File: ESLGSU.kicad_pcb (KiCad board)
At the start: 6 copper layers, 90.9 x 99.5 mm, 297 parts, among them J1 PJ-080BH, Q1 DMN67D7L-7, Q2 DMN67D7L-7, Q3 DMN67D7L-7, Q4 DMN67D7L-7, Q5 DMN67D7L-7, Q6 DMN67D7L-7, U1 TCA9544APWR, U10 TPS259474LRPWR, U11 LM73100RPWR, U12 MP28167-A, U13 INA219AIDCNR, U14 TPS259474LRPWR, U15 LM73100RPWR, U16 MP28167-A, U17 INA219AIDCNR, U18 TPS259474LRPWR, U19 LM73100RPWR, U2 DMT3006LDK-7, U20 MP28167-A, U21 INA219AIDCNR, U22 TPS259474LRPWR, U23 LM73100RPWR, U24 MP28167-A, U25 M20-7812045, U26 AP63203WU-7, U27 AP63205WU-7, U28 TPS2121RUXR, U29 TCAN1051GVDRBRQ, U3 INA219AIDCNR, U30 THVD1450DRBR, U31 TMUX1574RSVR, U32 TMUX1574RSVR, U33 TXU0202DTTR, U34 TMUX1574RSVR, U35 TXU0202DTTR, U36 TXB0104RUT, U37 STM32H753ZIT6, U38 STM32F072VBT6, U39 PCA9306, U4 DML3012LDC-7, U40 TXB0104RUT, U41 STM32F072CBUx, U44 TMUX1574RSVR, U46 TXB0104RUT, U47 TMUX1574RSVR, U5 AP74700QW6-7, U6 DMT3006LDK-7, U7 DML3012LDC-7, U8 AP74700QW6-7, U9 INA219AIDCNR

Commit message: Last tweaks on schematic
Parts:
- added C101: 22u, Capacitor_SMD:C_0805_2012Metric, F.Cu at (-123.8, -157.2)
- added C102: 100n, Capacitor_SMD:C_0402_1005Metric, F.Cu at (-121.5, -163.4)
- added C108: 100n, Capacitor_SMD:C_0402_1005Metric, F.Cu at (256.5, 49.3)
- added C109: 100n, Capacitor_SMD:C_0402_1005Metric, F.Cu at (256.5, 51.3)
- added C112: 100n, Capacitor_SMD:C_0402_1005Metric, F.Cu at (256.5, 53.2)
- added C113: 100n, Capacitor_SMD:C_0402_1005Metric, F.Cu at (256.5, 55.2)
- added C114: 100n, Capacitor_SMD:C_0402_1005Metric, F.Cu at (256.5, 57.2)
- added C115: 100p, Capacitor_SMD:C_0402_1005Metric, F.Cu at (256.5, 59.1)
- added C116: 2.2u, Capacitor_SMD:C_0402_1005Metric, F.Cu at (259.4, 49.3)
- added C117: 100n, Capacitor_SMD:C_0402_1005Metric, F.Cu at (259.4, 51.3)
- added C118: 100n, Capacitor_SMD:C_0402_1005Metric, F.Cu at (259.4, 53.2)
- added C119: 100n, Capacitor_SMD:C_0402_1005Metric, F.Cu at (259.4, 55.2)
- added C120: 4.7u, Capacitor_SMD:C_0402_1005Metric, F.Cu at (259.4, 57.2)
- added C121: 1u, Capacitor_SMD:C_0402_1005Metric, F.Cu at (259.4, 59.1)
- added C122: 100n, Capacitor_SMD:C_0402_1005Metric, F.Cu at (262.2, 49.3)
- added C123: 100n, Capacitor_SMD:C_0402_1005Metric, F.Cu at (262.2, 51.3)
- added C124: 100n, Capacitor_SMD:C_0402_1005Metric, F.Cu at (262.2, 53.2)
- added C125: 100n, Capacitor_SMD:C_0402_1005Metric, F.Cu at (262.2, 55.2)
- added C126: 100n, Capacitor_SMD:C_0402_1005Metric, F.Cu at (262.2, 57.2)
- added C127: 100n, Capacitor_SMD:C_0402_1005Metric, F.Cu at (249.5, 117.4)
- added C128: 100n, Capacitor_SMD:C_0402_1005Metric, F.Cu at (249.5, 119.4)
- added C129: 100n, Capacitor_SMD:C_0402_1005Metric, F.Cu at (249.5, 121.4)
- added C130: 100n, Capacitor_SMD:C_0402_1005Metric, F.Cu at (249.5, 123.3)
- added C131: 100n, Capacitor_SMD:C_0402_1005Metric, F.Cu at (249.5, 125.3)
- added C132: 100n, Capacitor_SMD:C_0402_1005Metric, F.Cu at (249.5, 127.3)
- added C133: 100n, Capacitor_SMD:C_0402_1005Metric, F.Cu at (249.5, 129.2)
- added C134: 100p, Capacitor_SMD:C_0402_1005Metric, F.Cu at (252.4, 117.4)
- added C135: 2.2u, Capacitor_SMD:C_0402_1005Metric, F.Cu at (252.4, 119.4)
- added C136: 100n, Capacitor_SMD:C_0402_1005Metric, F.Cu at (252.4, 121.4)
- added C137: 100n, Capacitor_SMD:C_0402_1005Metric, F.Cu at (252.4, 123.3)
- added C138: 100n, Capacitor_SMD:C_0402_1005Metric, F.Cu at (252.4, 125.3)
- added C139: 4.7u, Capacitor_SMD:C_0402_1005Metric, F.Cu at (252.4, 127.3)
- added C140: 1u, Capacitor_SMD:C_0402_1005Metric, F.Cu at (252.4, 129.2)
- added C141: 100n, Capacitor_SMD:C_0402_1005Metric, F.Cu at (255.3, 117.4)
- added C142: 100n, Capacitor_SMD:C_0402_1005Metric, F.Cu at (255.3, 119.4)
- added C143: 100n, Capacitor_SMD:C_0402_1005Metric, F.Cu at (255.3, 121.4)
- added C144: 100n, Capacitor_SMD:C_0402_1005Metric, F.Cu at (255.3, 123.3)
- added C145: 100n, Capacitor_SMD:C_0402_1005Metric, F.Cu at (255.3, 125.3)
- added C146: 100n, Capacitor_SMD:C_0402_1005Metric, F.Cu at (160.4, 69.4)
- added C147: 100n, Capacitor_SMD:C_0402_1005Metric, F.Cu at (160.4, 71.4)
- added C148: 100n, Capacitor_SMD:C_0402_1005Metric, F.Cu at (160.4, 73.3)
- added C149: 100n, Capacitor_SMD:C_0402_1005Metric, F.Cu at (160.4, 75.3)
- added C150: 100n, Capacitor_SMD:C_0402_1005Metric, F.Cu at (160.4, 77.3)
- added C151: 100n, Capacitor_SMD:C_0402_1005Metric, F.Cu at (160.4, 79.2)
- added C152: 100n, Capacitor_SMD:C_0402_1005Metric, F.Cu at (160.4, 81.2)
- added C153: 100n, Capacitor_SMD:C_0402_1005Metric, F.Cu at (160.4, 83.2)
- added C154: 100n, Capacitor_SMD:C_0402_1005Metric, F.Cu at (163.2, 69.4)
- added C155: 100n, Capacitor_SMD:C_0402_1005Metric, F.Cu at (163.2, 71.4)
- added C156: 100n, Capacitor_SMD:C_0402_1005Metric, F.Cu at (163.2, 73.3)
- added C157: 100n, Capacitor_SMD:C_0402_1005Metric, F.Cu at (163.2, 75.3)
- added C158: 100n, Capacitor_SMD:C_0402_1005Metric, F.Cu at (163.2, 77.3)
- added C159: 100p, Capacitor_SMD:C_0402_1005Metric, F.Cu at (163.2, 79.2)
- added C160: 100p, Capacitor_SMD:C_0402_1005Metric, F.Cu at (163.2, 81.2)
- added C161: 100n, Capacitor_SMD:C_0402_1005Metric, F.Cu at (163.2, 83.2)
- added C162: 100n, Capacitor_SMD:C_0402_1005Metric, F.Cu at (166.1, 69.4)
- added C163: 100n, Capacitor_SMD:C_0402_1005Metric, F.Cu at (166.1, 71.4)
- added C164: 100n, Capacitor_SMD:C_0402_1005Metric, F.Cu at (166.1, 73.3)
- added C165: 100n, Capacitor_SMD:C_0402_1005Metric, F.Cu at (166.1, 75.3)
- added C166: 100n, Capacitor_SMD:C_0402_1005Metric, F.Cu at (166.1, 77.3)
- added C167: 100n, Capacitor_SMD:C_0402_1005Metric, F.Cu at (166.1, 79.2)
- added C168: 100n, Capacitor_SMD:C_0402_1005Metric, F.Cu at (166.1, 81.2)
- added C169: 100n, Capacitor_SMD:C_0402_1005Metric, F.Cu at (166.1, 83.2)
- added C170: 100n, Capacitor_SMD:C_0402_1005Metric, F.Cu at (169.0, 69.4)
- added C171: 100n, Capacitor_SMD:C_0402_1005Metric, F.Cu at (169.0, 71.4)
- added C172: 100n, Capacitor_SMD:C_0402_1005Metric, F.Cu at (169.0, 73.3)
- added C173: 100n, Capacitor_SMD:C_0402_1005Metric, F.Cu at (169.0, 75.3)
- added C174: 100n, Capacitor_SMD:C_0402_1005Metric, F.Cu at (169.0, 77.3)
- added C175: 1u, Capacitor_SMD:C_0402_1005Metric, F.Cu at (169.0, 79.2)
- added C176: 100n, Capacitor_SMD:C_0402_1005Metric, F.Cu at (169.0, 81.2)
- added C177: 100n, Capacitor_SMD:C_0402_1005Metric, F.Cu at (169.0, 83.2)
- added C178: 4.7u, Capacitor_SMD:C_0402_1005Metric, F.Cu at (171.9, 69.4)
- added C179: 1u, Capacitor_SMD:C_0402_1005Metric, F.Cu at (171.9, 71.4)
- added C180: 100n, Capacitor_SMD:C_0402_1005Metric, F.Cu at (171.9, 73.3)
- added C181: 100n, Capacitor_SMD:C_0402_1005Metric, F.Cu at (171.9, 75.3)
- added C182: 100n, Capacitor_SMD:C_0402_1005Metric, F.Cu at (171.9, 77.3)
- added C183: 100n, Capacitor_SMD:C_0402_1005Metric, F.Cu at (171.9, 79.2)
- added C184: 100n, Capacitor_SMD:C_0402_1005Metric, F.Cu at (171.9, 81.2)
- added C185: 2.2u, Capacitor_SMD:C_0402_1005Metric, F.Cu at (171.9, 83.2)
- added C186: 2.2u, Capacitor_SMD:C_0402_1005Metric, F.Cu at (174.7, 69.4)
- added C187: 100n, Capacitor_SMD:C_0402_1005Metric, F.Cu at (174.7, 71.4)
- added C188: 100n, Capacitor_SMD:C_0402_1005Metric, F.Cu at (174.7, 73.3)
- added C189: 100n, Capacitor_SMD:C_0402_1005Metric, F.Cu at (174.7, 75.3)
- added C190: 100n, Capacitor_SMD:C_0402_1005Metric, F.Cu at (174.7, 77.3)
- added C191: 100n, Capacitor_SMD:C_0402_1005Metric, F.Cu at (174.7, 79.2)
- added C192: 100n, Capacitor_SMD:C_0402_1005Metric, F.Cu at (174.7, 81.2)
- added C193: 100n, Capacitor_SMD:C_0402_1005Metric, F.Cu at (174.7, 83.2)
- added C194: 100n, Capacitor_SMD:C_0402_1005Metric, F.Cu at (391.8, 101.6)
- added C195: 100n, Capacitor_SMD:C_0402_1005Metric, F.Cu at (391.8, 103.6)
- added C196: 100n, Capacitor_SMD:C_0402_1005Metric, F.Cu at (160.4, 127.5)
- added C197: 100n, Capacitor_SMD:C_0402_1005Metric, F.Cu at (160.4, 129.5)
- added C198: 100n, Capacitor_SMD:C_0402_1005Metric, F.Cu at (160.4, 131.4)
- added C199: 100n, Capacitor_SMD:C_0402_1005Metric, F.Cu at (160.4, 133.4)
- added C200: 100n, Capacitor_SMD:C_0402_1005Metric, F.Cu at (160.4, 135.4)
- added C201: 100n, Capacitor_SMD:C_0402_1005Metric, F.Cu at (160.4, 137.3)
- added C202: 100p, Capacitor_SMD:C_0402_1005Metric, F.Cu at (160.4, 139.3)
- added C203: 100n, Capacitor_SMD:C_0402_1005Metric, F.Cu at (163.2, 123.6)
- added C204: 100n, Capacitor_SMD:C_0402_1005Metric, F.Cu at (163.2, 125.5)
- added C205: 100n, Capacitor_SMD:C_0402_1005Metric, F.Cu at (163.2, 127.5)
- added C206: 100n, Capacitor_SMD:C_0402_1005Metric, F.Cu at (163.2, 129.5)
- added C207: 100n, Capacitor_SMD:C_0402_1005Metric, F.Cu at (163.2, 131.4)
- added C208: 100n, Capacitor_SMD:C_0402_1005Metric, F.Cu at (163.2, 133.4)
- added C209: 100n, Capacitor_SMD:C_0402_1005Metric, F.Cu at (163.2, 135.4)
- added C210: 100n, Capacitor_SMD:C_0402_1005Metric, F.Cu at (163.2, 137.3)
- added C211: 1u, Capacitor_SMD:C_0402_1005Metric, F.Cu at (163.2, 139.3)
- added C212: 100n, Capacitor_SMD:C_0402_1005Metric, F.Cu at (166.1, 123.6)
- added C213: 100n, Capacitor_SMD:C_0402_1005Metric, F.Cu at (166.1, 125.5)
- added C214: 4.7u, Capacitor_SMD:C_0402_1005Metric, F.Cu at (166.1, 127.5)
- added C215: 1u, Capacitor_SMD:C_0402_1005Metric, F.Cu at (166.1, 129.5)
- added C216: 100n, Capacitor_SMD:C_0402_1005Metric, F.Cu at (166.1, 131.4)
- added C217: 100n, Capacitor_SMD:C_0402_1005Metric, F.Cu at (166.1, 133.4)
- added C218: 100n, Capacitor_SMD:C_0402_1005Metric, F.Cu at (166.1, 135.4)
- added C219: 100n, Capacitor_SMD:C_0402_1005Metric, F.Cu at (166.1, 137.3)
- added C220: 100n, Capacitor_SMD:C_0402_1005Metric, F.Cu at (166.1, 139.3)
- added C221: 2.2u, Capacitor_SMD:C_0402_1005Metric, F.Cu at (169.0, 123.6)
- added C222: 2.2u, Capacitor_SMD:C_0402_1005Metric, F.Cu at (169.0, 125.5)
- added C223: 100n, Capacitor_SMD:C_0402_1005Metric, F.Cu at (169.0, 127.5)
- added C224: 100n, Capacitor_SMD:C_0402_1005Metric, F.Cu at (169.0, 129.5)
- added C225: 100n, Capacitor_SMD:C_0402_1005Metric, F.Cu at (169.0, 131.4)
- added C226: 100n, Capacitor_SMD:C_0402_1005Metric, F.Cu at (169.0, 133.4)
- added C227: 100n, Capacitor_SMD:C_0402_1005Metric, F.Cu at (169.0, 135.4)
- added C228: 100n, Capacitor_SMD:C_0402_1005Metric, F.Cu at (169.0, 137.3)
- added C229: 100n, Capacitor_SMD:C_0402_1005Metric, F.Cu at (169.0, 139.3)
- added C230: 100n, Capacitor_SMD:C_0402_1005Metric, F.Cu at (258.3, 101.0)
- added D10: TZ-P2-0603GTCS1-0.6T, LED_SMD:LED_0603_1608Metric, F.Cu at (258.6, 131.5)
- added D11: 1N5819, Diode_SMD:D_SOD-323, F.Cu at (185.2, 66.1)
- added D12: TZ-P2-0603GTCS1-0.6T, LED_SMD:LED_0603_1608Metric, F.Cu at (202.6, 78.0)
- added D13: 1N5819, Diode_SMD:D_SOD-323, F.Cu at (185.2, 116.3)
- added D14: TZ-P2-0603GTCS1-0.6T, LED_SMD:LED_0603_1608Metric, F.Cu at (194.5, 119.7)
- added D7: 1N5819, Diode_SMD:D_SOD-323, F.Cu at (245.3, 46.2)
- added D8: TZ-P2-0603GTCS1-0.6T, LED_SMD:LED_0603_1608Metric, F.Cu at (250.4, 65.5)
- added D9: 1N5819, Diode_SMD:D_SOD-323, F.Cu at (250.0, 114.3)
- added J10: 1054301108, ESLGSU_Parts_Lib:MOLEX_1054301108, F.Cu at (220.3, 129.6)
- added J2: XT60U-M, ESLGSU_Parts_Lib:XT60, F.Cu at (134.5, -164.7)
- added J3: Conn_01x06_Pin, Connector_PinHeader_1.27mm:PinHeader_1x06_P1.27mm_Vertical_SMD_Pin1Right, F.Cu at (259.1, 65.0)
- added J4: Conn_01x06_Pin, Connector_PinHeader_1.27mm:PinHeader_1x06_P1.27mm_Vertical_SMD_Pin1Right, F.Cu at (240.5, 133.0)
- added J5: 10118194-0001LF, ESLGSU_Parts_Lib:AMPHENOL_10118194-0001LF, F.Cu at (181.0, 73.2)
- added J6: Conn_01x06_Pin, Connector_PinHeader_1.27mm:PinHeader_1x06_P1.27mm_Vertical_SMD_Pin1Right, F.Cu at (180.2, 85.8)
- added J7: 10118194-0001LF, ESLGSU_Parts_Lib:AMPHENOL_10118194-0001LF, F.Cu at (185.8, 131.7)
- added J8: Conn_01x06_Pin, Connector_PinHeader_1.27mm:PinHeader_1x06_P1.27mm_Vertical_SMD_Pin1Right, F.Cu at (174.4, 139.5)
- added J9: AMPHENOL_62684-401100ALF, ESLGSU_Parts_Lib:AMPHENOL_62684-401100ALF, F.Cu at (220.5, 117.7)
- added L7: SRP1038A-4R7M, Inductor_SMD:L_Vishay_IHLP-4040, F.Cu at (-129.8, -164.5)
- added R101: 4.7K, Resistor_SMD:R_0402_1005Metric, F.Cu at (-121.5, -165.4)
- added R102: 200K, Resistor_SMD:R_0402_1005Metric, F.Cu at (244.9, 49.3)
- added R104: 0R, Resistor_SMD:R_0402_1005Metric, F.Cu at (244.9, 51.3)
- added R105: 100K, Resistor_SMD:R_0402_1005Metric, F.Cu at (244.9, 53.3)
- added R106: 200K, Resistor_SMD:R_0402_1005Metric, F.Cu at (244.9, 55.3)
- added R107: 200K, Resistor_SMD:R_0402_1005Metric, F.Cu at (244.9, 57.3)
- added R108: 200K, Resistor_SMD:R_0402_1005Metric, F.Cu at (244.9, 59.3)
- added R109: 0R, Resistor_SMD:R_0402_1005Metric, F.Cu at (244.9, 61.2)
- added R110: 0R, Resistor_SMD:R_0402_1005Metric, F.Cu at (244.9, 63.2)
- added R111: 0R, Resistor_SMD:R_0402_1005Metric, F.Cu at (247.8, 49.3)
- added R112: 510R, Resistor_SMD:R_0402_1005Metric, F.Cu at (247.8, 51.3)
- added R113: 0R, Resistor_SMD:R_0402_1005Metric, F.Cu at (247.8, 53.3)
- added R115: 200K, Resistor_SMD:R_0402_1005Metric, F.Cu at (247.8, 55.3)
- added R116: 200K, Resistor_SMD:R_0402_1005Metric, F.Cu at (247.8, 57.3)
- added R117: 200K, Resistor_SMD:R_0402_1005Metric, F.Cu at (247.8, 59.3)
- added R120: 10K, Resistor_SMD:R_0402_1005Metric, F.Cu at (247.8, 61.2)
- added R121: 0R, Resistor_SMD:R_0402_1005Metric, F.Cu at (247.8, 63.2)
- added R122: 10K, Resistor_SMD:R_0402_1005Metric, F.Cu at (250.7, 49.3)
- added R123: 10K, Resistor_SMD:R_0402_1005Metric, F.Cu at (250.7, 51.3)
- added R124: 510R, Resistor_SMD:R_0402_1005Metric, F.Cu at (250.7, 53.3)
- added R125: 0R, Resistor_SMD:R_0402_1005Metric, F.Cu at (250.7, 55.3)
- added R126: 200K, Resistor_SMD:R_0402_1005Metric, F.Cu at (250.7, 57.3)
- added R127: 100K, Resistor_SMD:R_0402_1005Metric, F.Cu at (250.7, 59.3)
- added R128: 200K, Resistor_SMD:R_0402_1005Metric, F.Cu at (250.7, 61.2)
- added R129: 200K, Resistor_SMD:R_0402_1005Metric, F.Cu at (250.7, 63.2)
- added R130: 33R, Resistor_SMD:R_0402_1005Metric, F.Cu at (253.6, 49.3)
- added R131: 200K, Resistor_SMD:R_0402_1005Metric, F.Cu at (253.6, 51.3)
- added R132: 510R, Resistor_SMD:R_0402_1005Metric, F.Cu at (253.6, 53.3)
- added R133: 0R, Resistor_SMD:R_0402_1005Metric, F.Cu at (253.6, 55.3)
- added R134: 0R, Resistor_SMD:R_0402_1005Metric, F.Cu at (253.6, 57.3)
- added R135: 200K, Resistor_SMD:R_0402_1005Metric, F.Cu at (237.9, 113.2)
- added R136: 120R, Resistor_SMD:R_0805_2012Metric, F.Cu at (250.3, 135.6)
- added R137: 0R, Resistor_SMD:R_0402_1005Metric, F.Cu at (237.9, 115.2)
- added R138: 100K, Resistor_SMD:R_0402_1005Metric, F.Cu at (237.9, 117.2)
- added R139: 200K, Resistor_SMD:R_0402_1005Metric, F.Cu at (237.9, 119.1)
- added R140: 200K, Resistor_SMD:R_0402_1005Metric, F.Cu at (237.9, 121.1)
- added R141: 200K, Resistor_SMD:R_0402_1005Metric, F.Cu at (237.9, 123.1)
- added R142: 0R, Resistor_SMD:R_0402_1005Metric, F.Cu at (237.9, 125.1)
- added R143: 0R, Resistor_SMD:R_0402_1005Metric, F.Cu at (237.9, 127.1)
- added R144: 0R, Resistor_SMD:R_0402_1005Metric, F.Cu at (240.8, 113.2)
- added R145: 510R, Resistor_SMD:R_0402_1005Metric, F.Cu at (240.8, 115.2)
- added R146: 0R, Resistor_SMD:R_0402_1005Metric, F.Cu at (240.8, 117.2)
- added R147: 100K, Resistor_SMD:R_0402_1005Metric, F.Cu at (240.8, 119.1)
- added R148: 200K, Resistor_SMD:R_0402_1005Metric, F.Cu at (240.8, 121.1)
- added R149: 200K, Resistor_SMD:R_0402_1005Metric, F.Cu at (240.8, 123.1)
- added R150: 200K, Resistor_SMD:R_0402_1005Metric, F.Cu at (240.8, 125.1)
- added R151: 200K, Resistor_SMD:R_0402_1005Metric, F.Cu at (240.8, 127.1)
- added R152: 10K, Resistor_SMD:R_0402_1005Metric, F.Cu at (243.7, 113.2)
- added R153: 10K, Resistor_SMD:R_0402_1005Metric, F.Cu at (243.7, 115.2)
- added R154: 0R, Resistor_SMD:R_0402_1005Metric, F.Cu at (243.7, 117.2)
- added R155: 10K, Resistor_SMD:R_0402_1005Metric, F.Cu at (243.7, 119.1)
- added R156: 10K, Resistor_SMD:R_0402_1005Metric, F.Cu at (243.7, 121.1)
- added R157: 510R, Resistor_SMD:R_0402_1005Metric, F.Cu at (243.7, 123.1)
- added R158: 0R, Resistor_SMD:R_0402_1005Metric, F.Cu at (243.7, 125.1)
- added R159: 200K, Resistor_SMD:R_0402_1005Metric, F.Cu at (243.7, 127.1)
- added R160: 100K, Resistor_SMD:R_0402_1005Metric, F.Cu at (246.7, 113.2)
- added R161: 200K, Resistor_SMD:R_0402_1005Metric, F.Cu at (246.7, 115.2)
- added R162: 200K, Resistor_SMD:R_0402_1005Metric, F.Cu at (246.7, 117.2)
- added R163: 33R, Resistor_SMD:R_0402_1005Metric, F.Cu at (246.7, 119.1)
- added R164: 200K, Resistor_SMD:R_0402_1005Metric, F.Cu at (246.7, 121.1)
- added R165: 510R, Resistor_SMD:R_0402_1005Metric, F.Cu at (246.7, 123.1)
- added R166: 0R, Resistor_SMD:R_0402_1005Metric, F.Cu at (246.7, 125.1)
- added R167: 0R, Resistor_SMD:R_0402_1005Metric, F.Cu at (246.7, 127.1)
- added R168: 120R, Resistor_SMD:R_0805_2012Metric, F.Cu at (171.7, 85.6)
- added R169: 120R, Resistor_SMD:R_0805_2012Metric, F.Cu at (171.7, 88.6)
- added R170: 100K, Resistor_SMD:R_0402_1005Metric, F.Cu at (184.8, 45.1)
- added R171: 100K, Resistor_SMD:R_0402_1005Metric, F.Cu at (184.8, 47.0)
- added R172: 100K, Resistor_SMD:R_0402_1005Metric, F.Cu at (184.8, 49.0)
- added R173: 200K, Resistor_SMD:R_0402_1005Metric, F.Cu at (184.8, 51.0)
- added R174: 200K, Resistor_SMD:R_0402_1005Metric, F.Cu at (184.8, 53.0)
- added R175: 200K, Resistor_SMD:R_0402_1005Metric, F.Cu at (184.8, 55.0)
- added R176: 10K, Resistor_SMD:R_0402_1005Metric, F.Cu at (184.8, 57.0)
- added R177: 10K, Resistor_SMD:R_0402_1005Metric, F.Cu at (184.8, 59.0)
- added R178: 120R, Resistor_SMD:R_0805_2012Metric, F.Cu at (171.7, 91.5)
- added R179: 120R, Resistor_SMD:R_0805_2012Metric, F.Cu at (171.7, 94.5)
- added R180: 200K, Resistor_SMD:R_0402_1005Metric, F.Cu at (184.8, 61.0)
- added R181: 200K, Resistor_SMD:R_0402_1005Metric, F.Cu at (184.8, 63.0)
- added R182: 100K, Resistor_SMD:R_0402_1005Metric, F.Cu at (187.7, 45.1)
- added R183: 200K, Resistor_SMD:R_0402_1005Metric, F.Cu at (187.7, 47.0)
- added R184: 100K, Resistor_SMD:R_0402_1005Metric, F.Cu at (187.7, 49.0)
- added R185: 200K, Resistor_SMD:R_0402_1005Metric, F.Cu at (187.7, 51.0)
- added R186: 200K, Resistor_SMD:R_0402_1005Metric, F.Cu at (187.7, 53.0)
- added R187: 200K, Resistor_SMD:R_0402_1005Metric, F.Cu at (187.7, 55.0)
- added R188: 200K, Resistor_SMD:R_0402_1005Metric, F.Cu at (187.7, 57.0)
- added R189: 200K, Resistor_SMD:R_0402_1005Metric, F.Cu at (187.7, 59.0)
- added R190: 10K, Resistor_SMD:R_0402_1005Metric, F.Cu at (187.7, 61.0)
- added R191: 10K, Resistor_SMD:R_0402_1005Metric, F.Cu at (187.7, 63.0)
- added R192: 10K, Resistor_SMD:R_0402_1005Metric, F.Cu at (190.6, 45.1)
- added R193: 10K, Resistor_SMD:R_0402_1005Metric, F.Cu at (190.6, 47.0)
- added R194: 10K, Resistor_SMD:R_0402_1005Metric, F.Cu at (190.6, 49.0)
- added R195: 10K, Resistor_SMD:R_0402_1005Metric, F.Cu at (190.6, 51.0)
- added R196: 10K, Resistor_SMD:R_0402_1005Metric, F.Cu at (190.6, 53.0)
- added R197: 10K, Resistor_SMD:R_0402_1005Metric, F.Cu at (190.6, 55.0)
- added R198: 0R, Resistor_SMD:R_0402_1005Metric, F.Cu at (190.6, 57.0)
- added R199: 200K, Resistor_SMD:R_0402_1005Metric, F.Cu at (190.6, 59.0)
- added R200: 200K, Resistor_SMD:R_0402_1005Metric, F.Cu at (190.6, 61.0)
- added R201: 33R, Resistor_SMD:R_0402_1005Metric, F.Cu at (190.6, 63.0)
- added R202: 100K, Resistor_SMD:R_0402_1005Metric, F.Cu at (193.5, 45.1)
- added R203: 100K, Resistor_SMD:R_0402_1005Metric, F.Cu at (193.5, 47.0)
- added R204: 0R, Resistor_SMD:R_0402_1005Metric, F.Cu at (193.5, 49.0)
- added R205: 200K, Resistor_SMD:R_0402_1005Metric, F.Cu at (193.5, 51.0)
- added R206: 200K, Resistor_SMD:R_0402_1005Metric, F.Cu at (193.5, 53.0)
- added R207: 0R, Resistor_SMD:R_0402_1005Metric, F.Cu at (193.5, 55.0)
- added R208: 200K, Resistor_SMD:R_0402_1005Metric, F.Cu at (193.5, 57.0)
- added R209: 200K, Resistor_SMD:R_0402_1005Metric, F.Cu at (193.5, 59.0)
- added R210: 200K, Resistor_SMD:R_0402_1005Metric, F.Cu at (193.5, 61.0)
- added R211: 200K, Resistor_SMD:R_0402_1005Metric, F.Cu at (193.5, 63.0)
- added R212: 510R, Resistor_SMD:R_0402_1005Metric, F.Cu at (196.4, 45.1)
- added R213: 0R, Resistor_SMD:R_0402_1005Metric, F.Cu at (196.4, 47.0)
- added R214: 0R, Resistor_SMD:R_0402_1005Metric, F.Cu at (196.4, 49.0)
- added R215: 200K, Resistor_SMD:R_0402_1005Metric, F.Cu at (196.4, 51.0)
- added R216: 200K, Resistor_SMD:R_0402_1005Metric, F.Cu at (196.4, 53.0)
- added R217: 100K, Resistor_SMD:R_0402_1005Metric, F.Cu at (196.4, 55.0)
- added R218: 100K, Resistor_SMD:R_0402_1005Metric, F.Cu at (196.4, 57.0)
- added R219: 200K, Resistor_SMD:R_0402_1005Metric, F.Cu at (196.4, 59.0)
- added R220: 200K, Resistor_SMD:R_0402_1005Metric, F.Cu at (196.4, 61.0)
- added R221: 200K, Resistor_SMD:R_0402_1005Metric, F.Cu at (196.4, 63.0)
- added R222: 0R, Resistor_SMD:R_0402_1005Metric, F.Cu at (199.3, 45.1)
- added R223: 510R, Resistor_SMD:R_0402_1005Metric, F.Cu at (199.3, 47.0)
- added R224: 0R, Resistor_SMD:R_0402_1005Metric, F.Cu at (199.3, 49.0)
- added R225: 200K, Resistor_SMD:R_0402_1005Metric, F.Cu at (199.3, 51.0)
- added R226: 200K, Resistor_SMD:R_0402_1005Metric, F.Cu at (199.3, 53.0)
- added R227: 0R, Resistor_SMD:R_0402_1005Metric, F.Cu at (199.3, 55.0)
- added R228: 510R, Resistor_SMD:R_0402_1005Metric, F.Cu at (199.3, 57.0)
- added R229: 0R, Resistor_SMD:R_0402_1005Metric, F.Cu at (199.3, 59.0)
- added R230: 10K, Resistor_SMD:R_0402_1005Metric, F.Cu at (74.6, 107.9)
- added R231: 10K, Resistor_SMD:R_0402_1005Metric, F.Cu at (74.6, 109.9)
- added R232: 120R, Resistor_SMD:R_0805_2012Metric, F.Cu at (430.9, 93.7)
- added R233: 100K, Resistor_SMD:R_0402_1005Metric, F.Cu at (184.8, 99.2)
- added R234: 100K, Resistor_SMD:R_0402_1005Metric, F.Cu at (416.2, 79.3)
- added R235: 200K, Resistor_SMD:R_0402_1005Metric, F.Cu at (184.8, 103.2)
- added R236: 200K, Resistor_SMD:R_0402_1005Metric, F.Cu at (416.2, 83.2)
- added R237: 10K, Resistor_SMD:R_0402_1005Metric, F.Cu at (184.8, 107.2)
- added R238: 120R, Resistor_SMD:R_0805_2012Metric, F.Cu at (199.4, 118.6)
- added R239: 200K, Resistor_SMD:R_0402_1005Metric, F.Cu at (184.8, 109.2)
- added R240: 100K, Resistor_SMD:R_0402_1005Metric, F.Cu at (184.8, 111.2)
- added R241: 200K, Resistor_SMD:R_0402_1005Metric, F.Cu at (184.8, 113.1)
- added R242: 200K, Resistor_SMD:R_0402_1005Metric, F.Cu at (187.7, 99.2)
- added R243: 200K, Resistor_SMD:R_0402_1005Metric, F.Cu at (187.7, 101.2)
- added R244: 200K, Resistor_SMD:R_0402_1005Metric, F.Cu at (187.7, 103.2)
- added R245: 10K, Resistor_SMD:R_0402_1005Metric, F.Cu at (187.7, 105.2)
- added R246: 10K, Resistor_SMD:R_0402_1005Metric, F.Cu at (187.7, 107.2)
- added R247: 10K, Resistor_SMD:R_0402_1005Metric, F.Cu at (187.7, 109.2)
- added R248: 10K, Resistor_SMD:R_0402_1005Metric, F.Cu at (187.7, 111.2)
- added R249: 0R, Resistor_SMD:R_0402_1005Metric, F.Cu at (187.7, 113.1)
- added R250: 200K, Resistor_SMD:R_0402_1005Metric, F.Cu at (190.6, 99.2)
- added R251: 33R, Resistor_SMD:R_0402_1005Metric, F.Cu at (190.6, 101.2)
- added R252: 100K, Resistor_SMD:R_0402_1005Metric, F.Cu at (190.6, 103.2)
- added R253: 0R, Resistor_SMD:R_0402_1005Metric, F.Cu at (190.6, 105.2)
- added R254: 200K, Resistor_SMD:R_0402_1005Metric, F.Cu at (190.6, 107.2)
- added R255: 0R, Resistor_SMD:R_0402_1005Metric, F.Cu at (190.6, 109.2)
- added R256: 200K, Resistor_SMD:R_0402_1005Metric, F.Cu at (190.6, 111.2)
- added R257: 200K, Resistor_SMD:R_0402_1005Metric, F.Cu at (190.6, 113.1)
- added R258: 200K, Resistor_SMD:R_0402_1005Metric, F.Cu at (193.5, 99.2)
- added R259: 510R, Resistor_SMD:R_0402_1005Metric, F.Cu at (193.5, 101.2)
- added R260: 0R, Resistor_SMD:R_0402_1005Metric, F.Cu at (193.5, 103.2)
- added R261: 0R, Resistor_SMD:R_0402_1005Metric, F.Cu at (193.5, 105.2)
- added R262: 200K, Resistor_SMD:R_0402_1005Metric, F.Cu at (193.5, 107.2)
- added R263: 100K, Resistor_SMD:R_0402_1005Metric, F.Cu at (193.5, 109.2)
- added R264: 200K, Resistor_SMD:R_0402_1005Metric, F.Cu at (193.5, 111.2)
- added R265: 0R, Resistor_SMD:R_0402_1005Metric, F.Cu at (193.5, 113.1)
- added R266: 510R, Resistor_SMD:R_0402_1005Metric, F.Cu at (196.4, 99.2)
- added R267: 10K, Resistor_SMD:R_0402_1005Metric, F.Cu at (196.4, 101.2)
- added R268: 10K, Resistor_SMD:R_0402_1005Metric, F.Cu at (196.4, 103.2)
- added R269: 200K, Resistor_SMD:R_0402_1005Metric, F.Cu at (196.4, 105.2)
- added R270: 0R, Resistor_SMD:R_0402_1005Metric, F.Cu at (196.4, 107.2)
- added R271: 510R, Resistor_SMD:R_0402_1005Metric, F.Cu at (196.4, 109.2)
- added R272: 200K, Resistor_SMD:R_0402_1005Metric, F.Cu at (255.4, 101.0)
- added R273: 200K, Resistor_SMD:R_0402_1005Metric, F.Cu at (255.4, 103.0)
- added R96: 4.7K, Resistor_SMD:R_0402_1005Metric, F.Cu at (40.1, -153.0)
- added R99: 4.7K, Resistor_SMD:R_0402_1005Metric, F.Cu at (-121.5, -167.4)
- added RN10: 0R, Resistor_SMD:R_Array_Convex_2x0402, F.Cu at (190.3, 69.9)
- added RN11: 0R, Resistor_SMD:R_Array_Convex_2x0402, F.Cu at (190.3, 72.8)
- added RN12: 0R, Resistor_SMD:R_Array_Convex_2x0402, F.Cu at (193.4, 69.9)
- added RN13: 10K, Resistor_SMD:R_Array_Convex_2x0402, F.Cu at (193.4, 72.8)
- added RN14: 0R, Resistor_SMD:R_Array_Convex_2x0402, F.Cu at (196.4, 69.9)
- added RN15: 10K, Resistor_SMD:R_Array_Convex_2x0402, F.Cu at (196.4, 72.8)
- added RN16: 0R, Resistor_SMD:R_Array_Convex_2x0402, F.Cu at (199.5, 69.9)
- added RN17: 0R, Resistor_SMD:R_Array_Convex_2x0402, F.Cu at (199.5, 72.8)
- added RN18: 0R, Resistor_SMD:R_Array_Concave_4x0402, F.Cu at (199.4, 93.5)
- added RN19: 0R, Resistor_SMD:R_Array_Concave_4x0402, F.Cu at (202.4, 93.5)
- added RN20: 0R, Resistor_SMD:R_Array_Convex_2x0402, F.Cu at (200.4, 128.3)
- added RN21: 0R, Resistor_SMD:R_Array_Concave_4x0402, F.Cu at (184.8, 120.2)
- added RN22: 0R, Resistor_SMD:R_Array_Concave_4x0402, F.Cu at (187.9, 120.2)
- added RN23: 0R, Resistor_SMD:R_Array_Convex_2x0402, F.Cu at (200.4, 131.3)
- added RN24: 0R, Resistor_SMD:R_Array_Convex_2x0402, F.Cu at (200.4, 134.2)
- added RN25: 10K, Resistor_SMD:R_Array_Convex_2x0402, F.Cu at (200.4, 137.2)
- added RN26: 0R, Resistor_SMD:R_Array_Convex_2x0402, F.Cu at (200.4, 140.1)
- added RN27: 0R, Resistor_SMD:R_Array_Concave_4x0402, F.Cu at (190.9, 120.2)
- added RN9: 0R, Resistor_SMD:R_Array_Concave_4x0402, F.Cu at (196.3, 93.5)
- added TP18: TestPoint, TestPoint:TestPoint_Pad_D1.5mm, F.Cu at (26.7, -140.4)
- added TP19: TestPoint, TestPoint:TestPoint_Pad_D1.5mm, F.Cu at (26.7, -136.9)
- added TP20: TestPoint, TestPoint:TestPoint_Pad_D1.5mm, F.Cu at (30.2, -140.4)
- added TP21: TestPoint, TestPoint:TestPoint_Pad_D1.5mm, F.Cu at (-131.4, -153.3)
- added TP22: TestPoint, TestPoint:TestPoint_Pad_D1.5mm, F.Cu at (-127.8, -156.9)
- added TP23: TestPoint, TestPoint:TestPoint_Pad_D1.5mm, F.Cu at (-127.8, -153.3)
- added TP24: TestPoint, TestPoint:TestPoint_Pad_D1.5mm, F.Cu at (265.4, 50.1)
- added TP25: TestPoint, TestPoint:TestPoint_Pad_D1.5mm, F.Cu at (265.4, 53.6)
- added TP26: TestPoint, TestPoint:TestPoint_Pad_D1.5mm, F.Cu at (265.4, 57.2)
- added TP27: TestPoint, TestPoint:TestPoint_Pad_D1.5mm, F.Cu at (258.5, 118.2)
- added TP28: TestPoint, TestPoint:TestPoint_Pad_D1.5mm, F.Cu at (258.5, 121.8)
- added TP29: TestPoint, TestPoint:TestPoint_Pad_D1.5mm, F.Cu at (258.5, 125.3)
- added TP30: TestPoint, TestPoint:TestPoint_Pad_D1.5mm, F.Cu at (202.5, 45.8)
- added TP31: TestPoint, TestPoint:TestPoint_Pad_D1.5mm, F.Cu at (202.5, 49.4)
- added TP32: TestPoint, TestPoint:TestPoint_Pad_D1.5mm, F.Cu at (202.5, 52.9)
- added TP33: TestPoint, TestPoint:TestPoint_Pad_D1.5mm, F.Cu at (199.6, 100.0)
- added TP34: TestPoint, TestPoint:TestPoint_Pad_D1.5mm, F.Cu at (199.6, 103.5)
- added TP35: TestPoint, TestPoint:TestPoint_Pad_D1.5mm, F.Cu at (199.6, 107.1)
- added U42: FXMA2102L8X, ESLGSU_Parts_Lib:UQFN8_MICROPAK, F.Cu at (258.0, 134.2)
- added U43: TMUX1574RSVR, ESLGSU_Parts_Lib:T-UQFN-16, F.Cu at (254.8, 132.4)
- added U45: TCAN1051GVDRBRQ, Package_DFN_QFN:DFN-8-1EP_3x3mm_P0.65mm_EP1.55x2.4mm, F.Cu at (186.9, 83.2)
- added U48: CY8C9520A, Package_SO:SSOP-28_5.3x10.2mm_P0.65mm, F.Cu at (164.2, 90.2)
- added U49: TXU0202DTTR, ESLGSU_Parts_Lib:SOT833-1-XSON8, F.Cu at (196.0, 90.0)
- added U50: TXU0202DTTR, ESLGSU_Parts_Lib:SOT833-1-XSON8, F.Cu at (198.5, 90.0)
- added U51: THVD1450DRBR, Package_DFN_QFN:DFN-8-1EP_3x3mm_P0.65mm_EP1.55x2.4mm, F.Cu at (186.9, 87.8)
- added U52: THVD1450DRBR, Package_DFN_QFN:DFN-8-1EP_3x3mm_P0.65mm_EP1.55x2.4mm, F.Cu at (186.9, 92.3)
- added U53: TMUX1574RSVR, ESLGSU_Parts_Lib:T-UQFN-16, F.Cu at (177.9, 78.8)
- added U54: ESD7004MUTAG, ESLGSU_Parts_Lib:UDFN10_ESD, F.Cu at (202.7, 61.7)
- added U55: PCAL6524HEAZ, Package_DFN_QFN:HVQFN-32-1EP_5x5mm_P0.5mm_EP3.1x3.1mm, F.Cu at (150.9, 78.0)
- added U56: TMUX1574RSVR, ESLGSU_Parts_Lib:T-UQFN-16, F.Cu at (181.4, 78.8)
- added U57: TMUX1574RSVR, ESLGSU_Parts_Lib:T-UQFN-16, F.Cu at (184.9, 78.8)
- added U58: FXMA2102L8X, ESLGSU_Parts_Lib:UQFN8_MICROPAK, F.Cu at (202.2, 56.1)
- added U59: FXMA2102L8X, ESLGSU_Parts_Lib:UQFN8_MICROPAK, F.Cu at (202.2, 59.0)
- added U60: TXU0202DTTR, ESLGSU_Parts_Lib:SOT833-1-XSON8, F.Cu at (200.9, 90.0)
- added U61: TXU0202DTTR, ESLGSU_Parts_Lib:SOT833-1-XSON8, F.Cu at (203.4, 90.0)
- added U62: TMUX1574RSVR, ESLGSU_Parts_Lib:T-UQFN-16, F.Cu at (188.3, 78.8)
- added U63: TMUX1574RSVR, ESLGSU_Parts_Lib:T-UQFN-16, F.Cu at (191.8, 78.8)
- added U64: STM32H743ZITx, Package_QFP:LQFP-144_20x20mm_P0.5mm, F.Cu at (171.1, 56.2)
- added U65: TPS2115ADRBR, Package_SON:VSON-8-1EP_3x3mm_P0.65mm_EP1.65x2.4mm_ThermalVias, F.Cu at (192.2, 83.2)
- added U66: TXB0104RUT, ESLGSU_Parts_Lib:T-UQFN-12, F.Cu at (198.9, 65.9)
- added U67: TXB0104RUT, ESLGSU_Parts_Lib:T-UQFN-12, F.Cu at (202.4, 65.9)
- added U68: TMUX1574RSVR, ESLGSU_Parts_Lib:T-UQFN-16, F.Cu at (195.3, 78.8)
- added U69: TMUX1574RSVR, ESLGSU_Parts_Lib:T-UQFN-16, F.Cu at (198.8, 78.8)
- added U70: TPS2115ADRBR, Package_SON:VSON-8-1EP_3x3mm_P0.65mm_EP1.65x2.4mm_ThermalVias, F.Cu at (192.2, 87.8)
- added U71: TPS2115ADRBR, Package_SON:VSON-8-1EP_3x3mm_P0.65mm_EP1.65x2.4mm_ThermalVias, F.Cu at (192.2, 92.3)
- added U72: FH-00339, ESLGSU_Parts_Lib:PI_ZERO_2_W, F.Cu at (70.4, 128.2)
- added U73: TCAN1051GVDRBRQ, Package_DFN_QFN:DFN-8-1EP_3x3mm_P0.65mm_EP1.55x2.4mm, F.Cu at (422.4, 115.4)
- added U74: TMUX1574RSVR, ESLGSU_Parts_Lib:T-UQFN-16, F.Cu at (182.7, 124.7)
- added U75: CY8C9520A, Package_SO:SSOP-28_5.3x10.2mm_P0.65mm, F.Cu at (175.7, 128.6)
- added U76: TXU0202DTTR, ESLGSU_Parts_Lib:SOT833-1-XSON8, F.Cu at (160.2, 142.0)
- added U77: THVD1450DRBR, Package_DFN_QFN:DFN-8-1EP_3x3mm_P0.65mm_EP1.55x2.4mm, F.Cu at (190.9, 141.9)
- added U78: TMUX1574RSVR, ESLGSU_Parts_Lib:T-UQFN-16, F.Cu at (186.2, 124.7)
- added U79: PCAL6524HEAZ, Package_DFN_QFN:HVQFN-32-1EP_5x5mm_P0.5mm_EP3.1x3.1mm, F.Cu at (184.6, 138.7)
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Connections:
- C10 pad 1: Net-(U2-D) -> Net-(U4-SR)
- C10 pad 2: GNDA -> GND
- C100 pad 1: /Main_uC/VBUS -> Net-(U26-IN)
- C103 pad 1: GND -> /BUS_UNREG
- C103 pad 2: Net-(U39-VREF2) -> GND
- C104 pad 1: GND -> Net-(U27-dVdt)
- C104 pad 2: /Main_uC/VBUS -> GND
- C105 pad 1: GND -> Net-(U27-ITIMER)
- C105 pad 2: /Main_uC/VBUS -> GND
- C106 pad 1: GND -> Net-(U26-IN)
- C106 pad 2: /Main_uC/SYS_3V3 -> GND
- C107 pad 1: GND -> Net-(U28-VCC)
- C107 pad 2: /Main_uC/SYS_3V3 -> GND
- C11 pad 1: Net-(U7-SR) -> Net-(U5-VCAP)
- C11 pad 2: GNDA -> GND
- C110 pad 2: /Main_uC/VBUS -> /BUS_3V3
- C111 pad 2: /Main_uC/SYS_3V3 -> /SYS_5V
- C12 pad 1: Net-(U8-VCAP) -> Net-(U7-SW1)
- C12 pad 2: GNDA -> Net-(C12-Pad2)
- C13 pad 1: Net-(U12-SW1) -> Net-(U7-SW2)
- C14 pad 1: Net-(U12-SW2) -> Net-(U7-CFLR)
- C14 pad 2: Net-(C14-Pad2) -> GND
- C15 pad 1: /SYS_3V3 -> Net-(U7-CFLR)
- C16 pad 1: Net-(U10-OUT) -> /SYS_5V
- C16 pad 2: GNDA -> GND
- C17 pad 1: Net-(U10-OUT) -> Net-(C17-Pad1)
- C17 pad 2: GNDA -> Net-(U7-SRN)
- C18 pad 1: Net-(U10-OUT) -> Net-(U7-IN)
- C18 pad 2: GNDA -> GND
- C19 pad 1: Net-(U12-OC) -> Net-(U7-IN)
- C19 pad 2: GNDA -> GND
- C2 pad 2: GNDA -> GND
- C20 pad 1: Net-(U11-IN) -> Net-(U6-S)
- C20 pad 2: GNDA -> GND
- C21 pad 1: Net-(U11-IN) -> Net-(U2-D)
- C21 pad 2: GNDA -> GND
- C22 pad 1: Net-(U11-IN) -> /System_Power/VBAT
- C22 pad 2: GNDA -> GND
- C23 pad 1: Net-(U11-IN) -> /System_Power/VBAT
- C23 pad 2: GNDA -> GND
- C24 pad 1: Net-(U11-IN) -> Net-(U8-SR)
- C24 pad 2: GNDA -> GND
- C25 pad 1: Net-(U11-IN) -> Net-(U9-VCAP)
- C25 pad 2: GNDA -> GND
- C26 pad 1: /BUS_UNREG -> Net-(C26-Pad1)
- C26 pad 2: GNDA -> GND
- C27 pad 1: Net-(U10-dVdt) -> Net-(U10-BST)
- C27 pad 2: GNDA -> Net-(U10-SW)
- C28 pad 1: Net-(U10-ITIMER) -> /SYS_5V
- C28 pad 2: GNDA -> GND
- C29 pad 1: Net-(U11-IN) -> /SYS_5V
- C29 pad 2: GNDA -> GND
- C30 pad 1: Net-(U12-VCC) -> Net-(U10-EN)
- C30 pad 2: GNDA -> GND
- C31 pad 1: Net-(U16-SW1) -> Net-(U11-SS)
- C31 pad 2: Net-(C31-Pad2) -> GND
- C32 pad 1: Net-(U16-SW2) -> Net-(U12-BST)
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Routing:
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- removed copper zone on B.Cu, net (none)
- removed copper zone on F.Cu, net (none)
- removed copper zone on B.Cu, net /BUS_3V3
- removed copper zone on F.Cu, net /BUS_3V3
- removed copper zone on B.Cu, net /BUS_UNREG
- removed copper zone on F.Cu, net /BUS_UNREG
- removed copper zone on In2.Cu, net /BUS_UNREG
- removed copper zone on In2.Cu, net /Main_uC/SYS_3V3
- removed copper zone on B.Cu, net /SYS_5V
- removed copper zone on F.Cu, net /SYS_5V
- removed copper zone on B.Cu, net GNDA
- removed copper zone on F.Cu, net GNDA
- removed copper zone on In1.Cu, net GNDA
- removed copper zone on In4.Cu, net GNDA
- removed copper zone on B.Cu, net Net-(U10-OUT)
- removed copper zone on F.Cu, net Net-(U10-OUT)
- removed copper zone on B.Cu, net Net-(U11-IN)
- removed copper zone on F.Cu, net Net-(U11-IN)
- removed copper zone on B.Cu, net Net-(U11-OUT)
- removed copper zone on F.Cu, net Net-(U11-OUT)
- removed copper zone on F.Cu, net Net-(U12-SW1)
- removed copper zone on F.Cu, net Net-(U12-SW2)
- removed copper zone on B.Cu, net Net-(U14-OUT)
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
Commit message: Some PCB work
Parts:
- moved U31 530.7 mm to (552.1, 400.4)
- moved U37 476.5 mm to (539.8, 67.0)
- moved R103 473.0 mm to (566.6, 66.8), turned to -90 degrees
- moved C116 472.7 mm to (589.0, 388.1)
- moved C120 472.7 mm to (589.0, 396.0)
- moved C121 472.7 mm to (589.0, 398.0)
- moved C122 472.7 mm to (591.9, 388.1)
- moved C123 472.7 mm to (591.9, 390.1)
- moved C124 472.7 mm to (591.9, 392.0)
- moved C125 472.7 mm to (591.9, 394.0)
- moved C126 472.7 mm to (591.9, 396.0)
- moved R102 472.7 mm to (574.5, 388.1)
- moved R104 472.7 mm to (574.5, 390.1)
- moved R109 472.7 mm to (574.5, 400.1)
- moved R110 472.7 mm to (574.5, 402.0)
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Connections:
- U54 pad 10: unconnected-(U54-NC1-Pad10) -> /Main_uC/USB_VBUS
- U54 pad 6: unconnected-(U54-NC4-Pad6) -> /Main_uC/USB_ID
- U54 pad 7: unconnected-(U54-NC3-Pad7) -> /Main_uC/USB_D+
- U54 pad 9: unconnected-(U54-NC2-Pad9) -> /Main_uC/USB_D-
- U55 pad 19: /Main_uC/nVBUS -> /Main_uC/nVSYS
- U55 pad 20: /Main_uC/nVSYS -> /Main_uC/nVBUS
- U79 pad 13: unconnected-(U79-P1_4-Pad13) -> /RAW_PIN_BUS
- U79 pad 15: /EPS_uC/RAW_PIN_BAT -> unconnected-(U79-P1_6-Pad15)
- U79 pad 19: /EPS_uC/GPIO_nEN -> /EPS_uC/nVSYS
- U79 pad 20: /EPS_uC/nVSYS -> /EPS_uC/GPIO_nEN
- U80 pad 10: unconnected-(U80-NC1-Pad10) -> /EPS_uC/USB_VBUS
- U80 pad 6: unconnected-(U80-NC4-Pad6) -> /EPS_uC/USB_ID
- U80 pad 7: unconnected-(U80-NC3-Pad7) -> /EPS_uC/USB_D+
- U80 pad 9: unconnected-(U80-NC2-Pad9) -> /EPS_uC/USB_D-
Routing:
- net /SYS_3V3: track 0.00 -> 110.4 mm, vias 0 -> 16
- net /CFGI2C_SDA: track 0.00 -> 57.4 mm, vias 0 -> 6
- net /CFGI2C_SCL: track 0.00 -> 54.9 mm, vias 0 -> 6
- net /EPS_uC/SUB3V3: track 0.00 -> 41.9 mm, vias 0 -> 20
- net /Main_uC/SUB3V3: track 0.00 -> 41.8 mm, vias 0 -> 19
- net GND: track 0.00 -> 31.2 mm, vias 0 -> 123
- net /Main_uC/RS4852_EN: track 0.00 -> 26.5 mm, vias 0 -> 1
- net /Main_uC/RS4851_EN: track 0.00 -> 26.4 mm, vias 0 -> 1
- net /EPS_uC/RS4851_EN: track 0.00 -> 26.3 mm, vias 0 -> 1
- net /Main_uC/CAN2_SE: track 0.00 -> 26.0 mm
- net /Misc_uC_Combined/UC1_CANSE: track 0.00 -> 26.0 mm
- net /Main_uC/CAN1_SE: track 0.00 -> 26.0 mm
- net /EPS_uC/CAN1_SE: track 0.00 -> 26.0 mm
- net /Misc_uC_Combined/UC1_NVT5V: track 0.00 -> 22.3 mm
- net /Main_uC/I2C1_nPEN: track 0.00 -> 22.3 mm
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
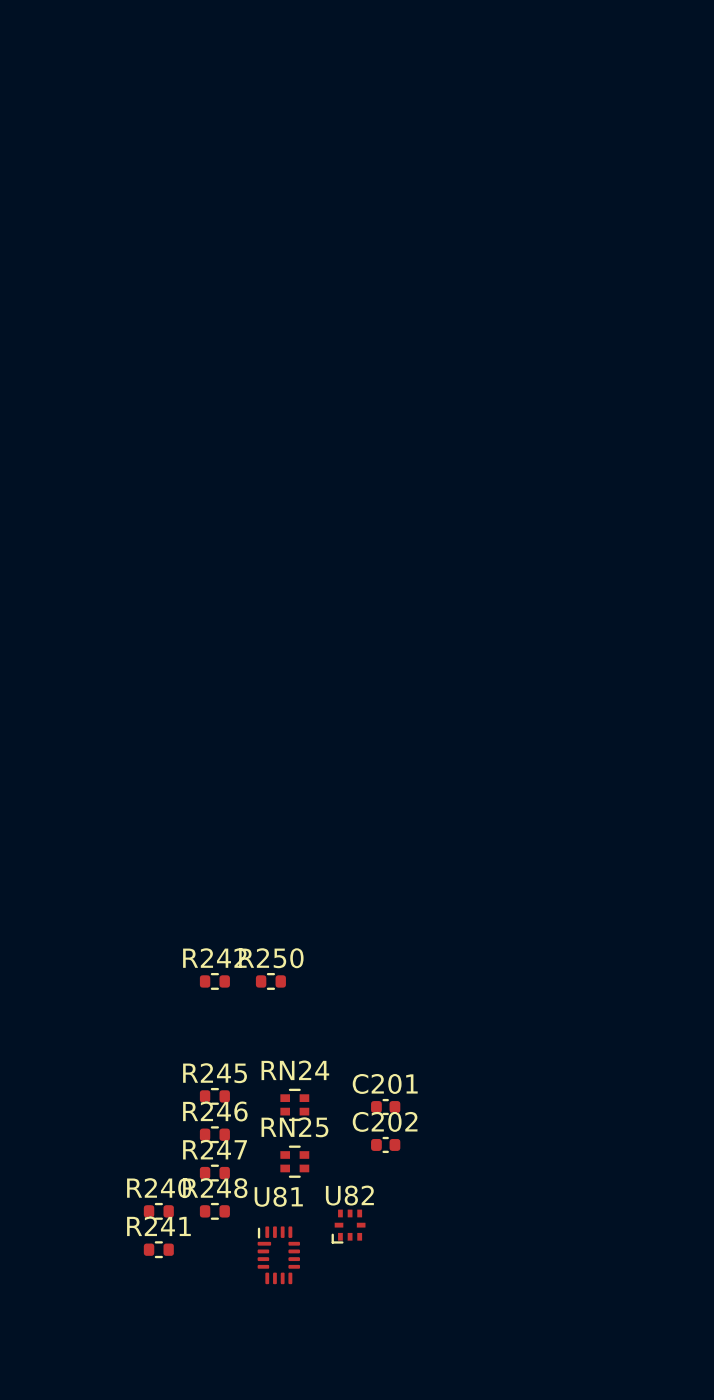
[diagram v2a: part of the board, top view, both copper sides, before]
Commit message: I2C interfaces PCB
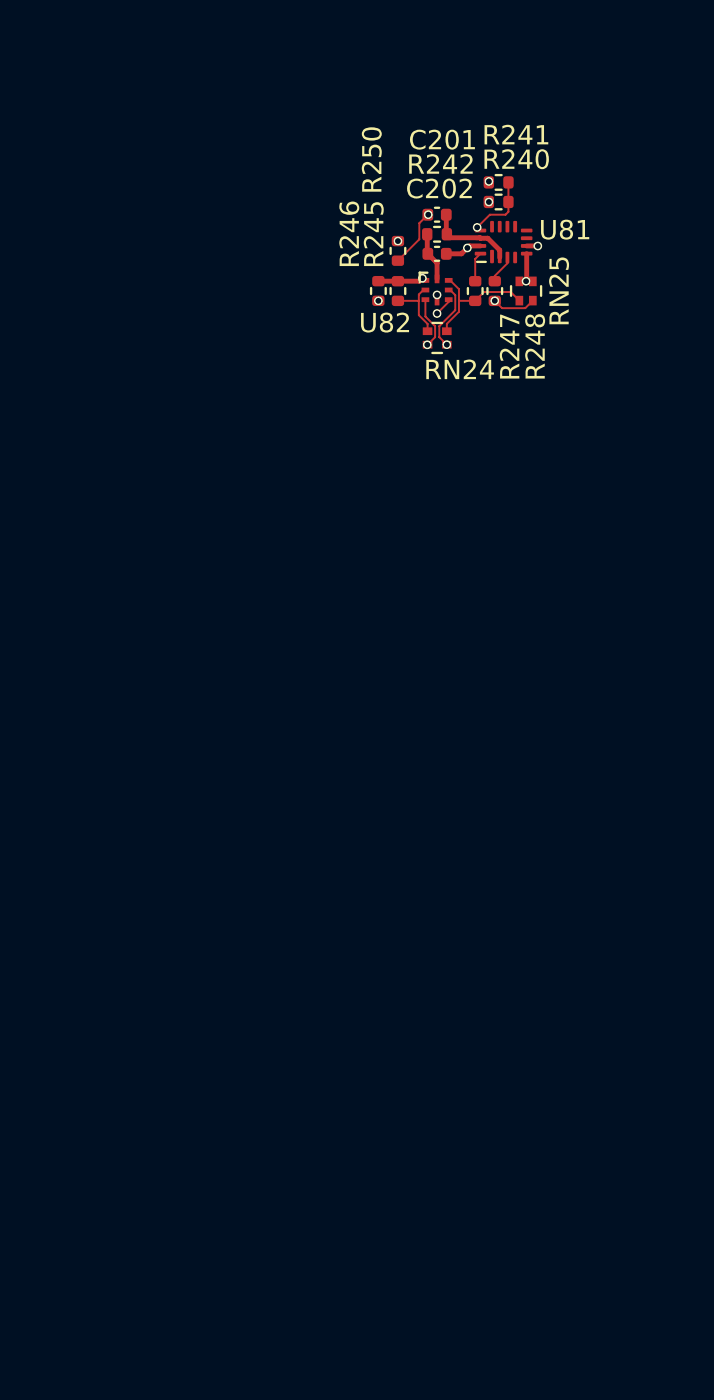
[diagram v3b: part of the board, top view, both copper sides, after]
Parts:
- moved R241 58.2 mm to (539.6, 89.0), turned to 180 degrees
- moved R240 55.3 mm to (539.6, 90.0), turned to 180 degrees
- moved U81 53.9 mm to (539.8, 92.1), turned to 90 degrees
- moved R248 50.0 mm to (539.4, 94.7), turned to -90 degrees
- moved U82 48.8 mm to (536.4, 94.6), turned to -90 degrees
- moved R247 47.8 mm to (538.4, 94.7), turned to -90 degrees
- moved RN25 46.8 mm to (541.0, 94.7), turned to -90 degrees
- moved C201 46.4 mm to (536.4, 90.7), turned to 180 degrees
- moved C202 46.4 mm to (536.4, 92.7), turned to 180 degrees
- moved R246 44.6 mm to (533.3, 94.7), turned to -90 degrees
- moved R245 42.9 mm to (534.4, 94.7), turned to -90 degrees
- moved RN24 40.5 mm to (536.4, 97.1), turned to 180 degrees
- moved R242 40.5 mm to (536.4, 91.7), turned to 180 degrees
- moved R250 38.5 mm to (534.4, 92.6), turned to -90 degrees
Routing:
- net /I2C1_SDA: track 0.00 -> 9.27 mm, vias 0 -> 2
- net /I2C1_SCL: track 0.00 -> 6.68 mm
- net /EPS_uC/VBUS: track 8.25 -> 14.9 mm, vias 2 -> 4
- net /EPS_uC/_I2C1_SDA: track 0.00 -> 6.25 mm, vias 0 -> 2
- net /EPS_uC/I2C1_EN: track 22.1 -> 27.7 mm, vias 0 -> 2
- net GND: track 31.2 -> 36.8 mm, vias 123 -> 128
- net /EPS_uC/I2C1_nPEN: track 22.2 -> 25.9 mm, vias 0 -> 1
- net /EPS_uC/_I2C1_SCL: track 0.00 -> 3.62 mm
- net /EPS_uC/SUB3V3: track 41.9 -> 44.5 mm, vias 20 -> 21
- net Net-(U82-VREF2): track 0.00 -> 2.53 mm
- net Net-(U81-S1A): track 0.00 -> 1.55 mm
- net Net-(U81-S2A): track 0.00 -> 1.50 mm
